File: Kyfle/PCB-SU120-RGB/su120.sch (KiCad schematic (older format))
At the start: 83 parts, among them J1 MJ-4PP-9, J2 Conn_01x03, J3 Conn_01x08, J4 Conn_01x08, J6 MJ-4PP-9, SW1 SW_PUSH_LED, SW10 SW_PUSH_LED, SW11 SW_PUSH_LED, SW12 SW_PUSH_LED, SW13 SW_PUSH_LED, SW14 SW_PUSH_LED, SW15 SW_PUSH_LED, SW16 SW_PUSH_LED, SW17 SW_PUSH_LED, SW18 SW_PUSH_LED, SW19 Rotary_Encoder_Switch, SW2 SW_PUSH_LED, SW20 Rotary_Encoder_Switch, SW21 Rotary_Encoder_Switch, SW22 SW_Push, SW23 Rotary_Encoder_Switch, SW3 SW_PUSH_LED, SW4 SW_PUSH_LED, SW5 SW_PUSH_LED, SW6 SW_PUSH_LED, SW7 SW_PUSH_LED, SW8 SW_PUSH_LED, SW9 SW_PUSH_LED, U1 ProMicro

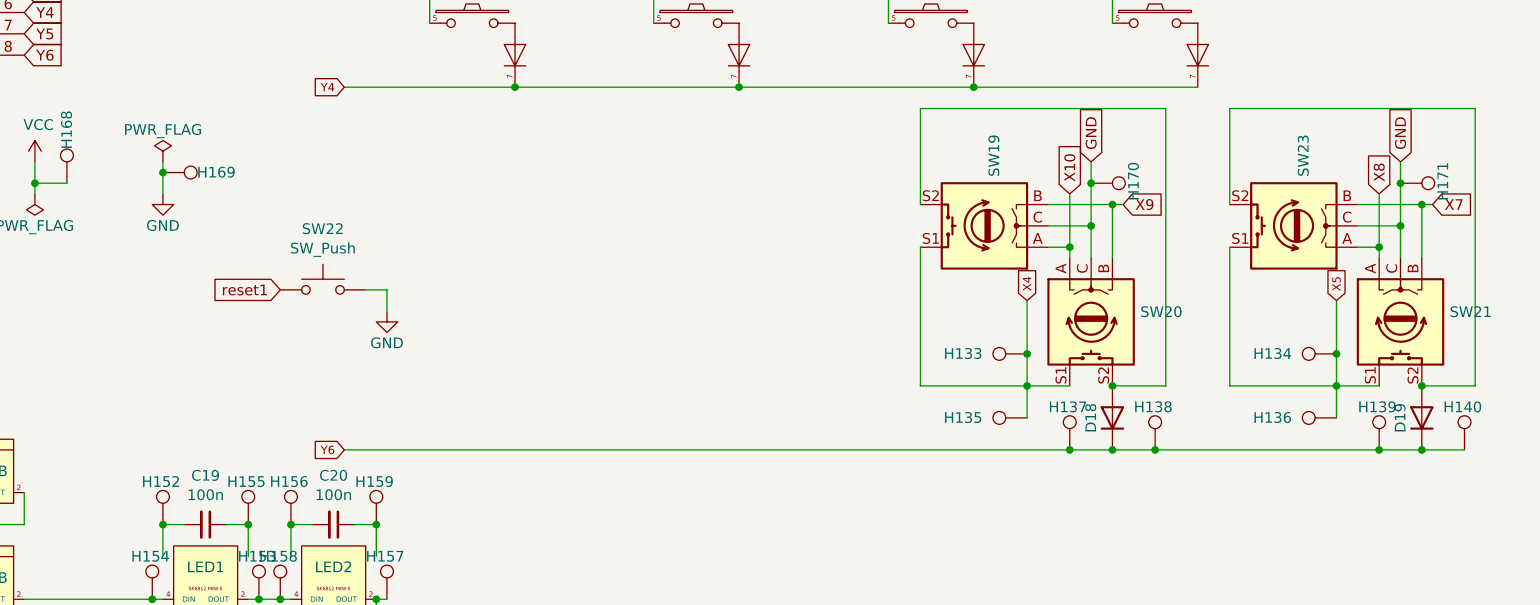
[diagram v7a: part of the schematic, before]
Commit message: Tentative routing of the 5-way switch
Not yet integrated in the main board itself.
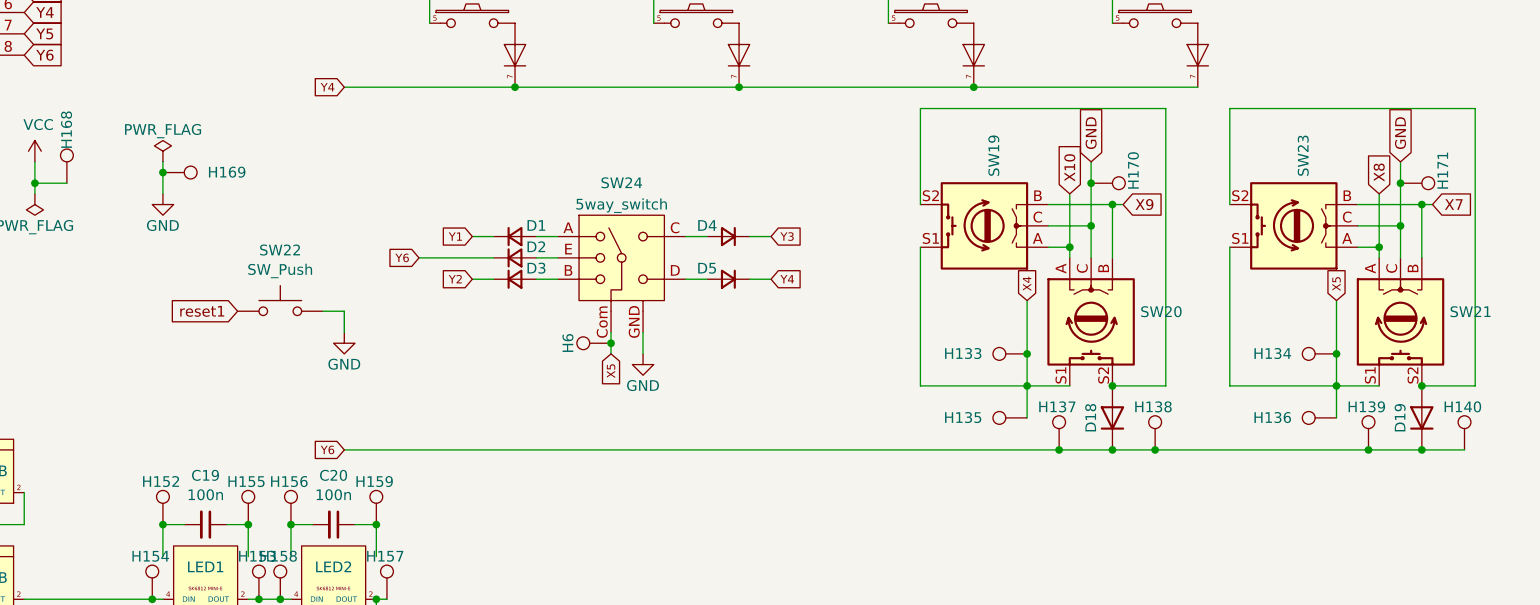
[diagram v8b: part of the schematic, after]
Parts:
- added D1, D2, D3, D4, D5: D_Small, Kyfle Footprints:diode_TH_SMD_rev3, symbol Device:D_Small
- added H6: MountingHole_Pad, Kyfle Footprints:1pin_rect_conn, symbol Connector:TestPoint
- added SW24: 5way_switch, Kyfle Footprints:Five_Way_Switch_Panasonic_EVQQ7, symbol #library:5way_switch
- C19, C20, C21, C22: footprint #footprint:C_0603_0805_HandSolder -> Kyfle Footprints:C_0603_0805_HandSolder
- D18, D19: footprint #footprint:diode_TH_SMD_rev2 -> Kyfle Footprints:diode_TH_SMD_rev3
- H133, H134, H135, H136, H137, H138, H139, H140, H46, H50: footprint #footprint:1pad_conn -> Kyfle Footprints:1pin_rect_conn
- H152, H155, H156, H159, H160, H163, H164, H167, H57: footprint #footprint:1pin_conn -> Kyfle Footprints:1pin_conn
- H153, H154, H157, H158, H161, H162, H165, H166, H168, H169: footprint #footprint:1pad_conn -> Kyfle Footprints:1pad_conn
- H170, H171: footprint #footprint:1pin_conn -> Kyfle Footprints:1pin_rect_conn
- J1, J6: footprint #footprint:MJ-4PP-9 -> Kyfle Footprints:MJ-4PP-9
- J2: footprint #footprint:PinHeader_1x03_P2.54mm_Vertical -> Kyfle Footprints:PinHeader_1x03_P2.54mm_Vertical
- J3, J4: footprint #footprint:PinHeader_1x08_P2.54mm_Vertical_rev2 -> Kyfle Footprints:PinHeader_1x08_P2.54mm_Vertical_rev2
- JP101, JP102, JP103, JP104, JP105, JP106, JP107, JP108: footprint #footprint:SolderJumper-3_P1.3mm_Open_TrianglePad1.0x1.5mm_duplex -> Kyfle Footprints:SolderJumper-3_P1.3mm_Open_TrianglePad1.0x1.5mm_duplex
- LED1, LED2, LED3, LED4: footprint #footprint:SK6812_Mini_E -> Kyfle Footprints:SK6812_Mini_E
- SW1, SW10, SW11, SW12, SW13, SW14, SW15, SW16, SW2, SW3, SW4, SW5, SW6, SW7, SW8, SW9: footprint #footprint:CherryMX_MidHeight_RGB_Hotswap_v2 -> Kyfle Footprints:CherryMX_Kyfle_v1_Module
- SW17, SW18: footprint #footprint:CherryMX_MidHeight_RGB_Hotswap_v2 -> Kyfle Footprints:CherryMX_Kyfle_v1_Module_For_Rotated
- SW19, SW23: footprint Kyfle Footprints:RollerEncoder_Panasonic_EVQWGD001 -> Kyfle Footprints:RollerEncoder_Panasonic_EVQWGD001_No_Cutout
- SW20, SW21: footprint #footprint:RotaryEncoder_Alps_EC11E-Switch_Vertical_H20mm_rev2 -> Kyfle Footprints:RotaryEncoder_Alps_EC11E-Switch_Vertical_H20mm_rev2
- SW22: footprint #footprint:ResetSW -> Kyfle Footprints:ResetSW
- U1: footprint #footprint:ArduinoProMicro-Rivets -> Kyfle Footprints:Arduino_ProMicro_Rivets
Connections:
- net GND: now also SW24.GND
- net X5: now also H6.1, SW24.Com
- net Y1: now also D1.1 (K)
- net Y2: now also D3.1 (K)
- net Y3: now also D4.1 (K)
- net Y4: now also D5.1 (K)
- net Y6: now also D2.1 (K)
- new net: D1.2 (A), SW24.A
- new net: D3.2 (A), SW24.B
- new net: D4.2 (A), SW24.C
- new net: D5.2 (A), SW24.D
- new net: D2.2 (A), SW24.E
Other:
- moved on the sheet: H137, H139, SW22
